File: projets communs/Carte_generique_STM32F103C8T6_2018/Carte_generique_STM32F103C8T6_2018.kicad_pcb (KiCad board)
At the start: 2 copper layers, 26 parts, among them J1 Conn_01x20_Female, J2 Alim puissance, J3 Alim logique, J4 Conn_01x20_Female, J5 PWM input, J6 PWM output, J7 QEI, J8 Liaison serie, Q1 PMF370XN, Q2 2N7000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

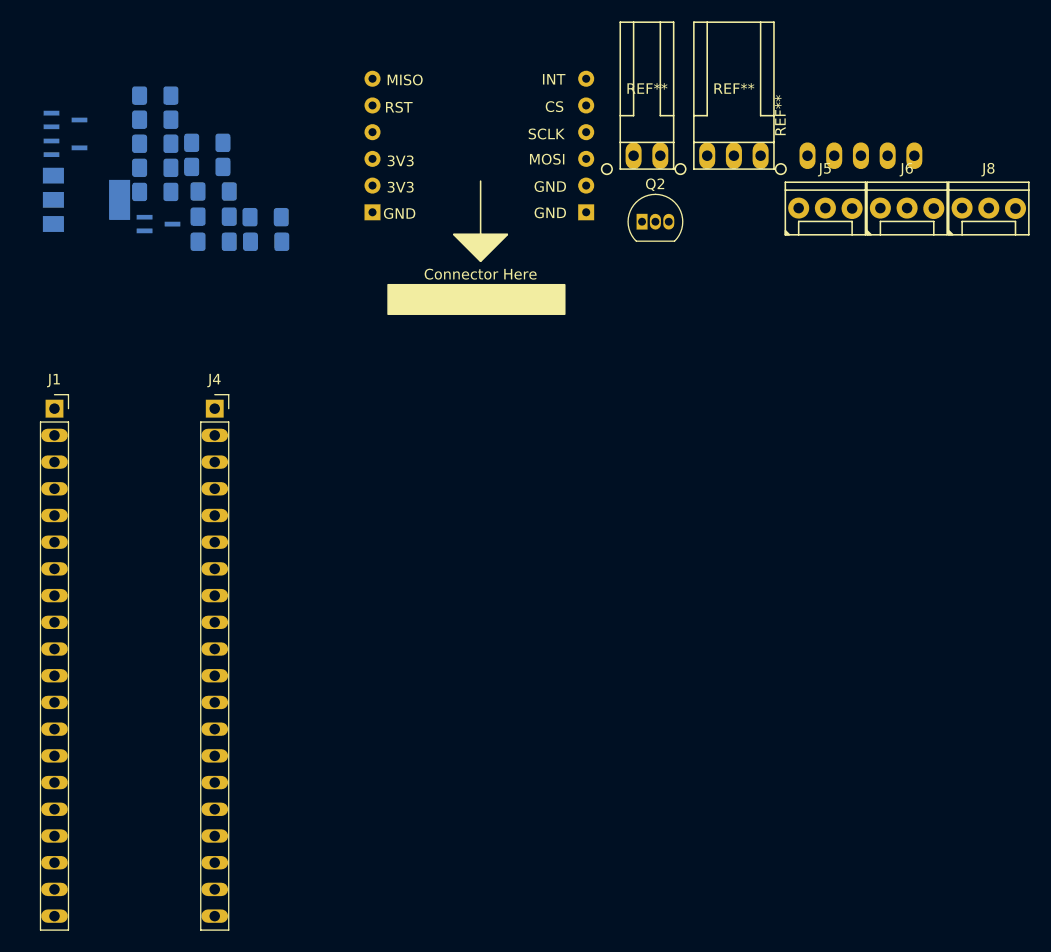
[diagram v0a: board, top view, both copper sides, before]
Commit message: added the blackpill actual courtyard
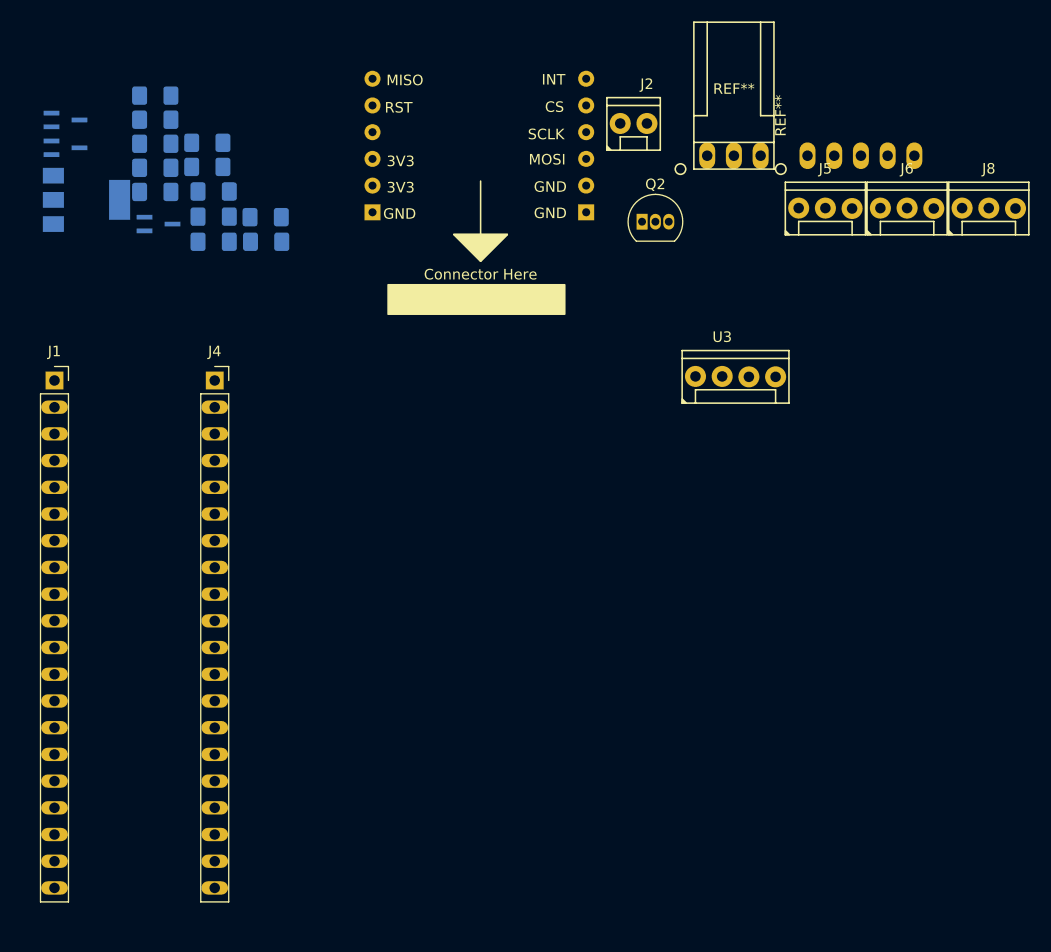
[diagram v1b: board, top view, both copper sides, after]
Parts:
- added U3: servo_connector, @Robot:HE14-4-straight, F.Cu at (180.3, 74.9)
- J2: footprint @Robot:HE14-2_horizontal -> @Robot:HE14-2-straight
- R2, R3: value R -> 10k
- moved J1 2.68 mm to (116.8, 76.1)
- moved J4 2.68 mm to (132.1, 76.1)
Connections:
- J1 pad 20: +3V3 -> Net-(J1-Pad20)
- J4 pad 3: +3V3 -> Net-(J4-Pad3)
- Q3 pad 1: /TX -> /led_communication

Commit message: changed the power connector footprint
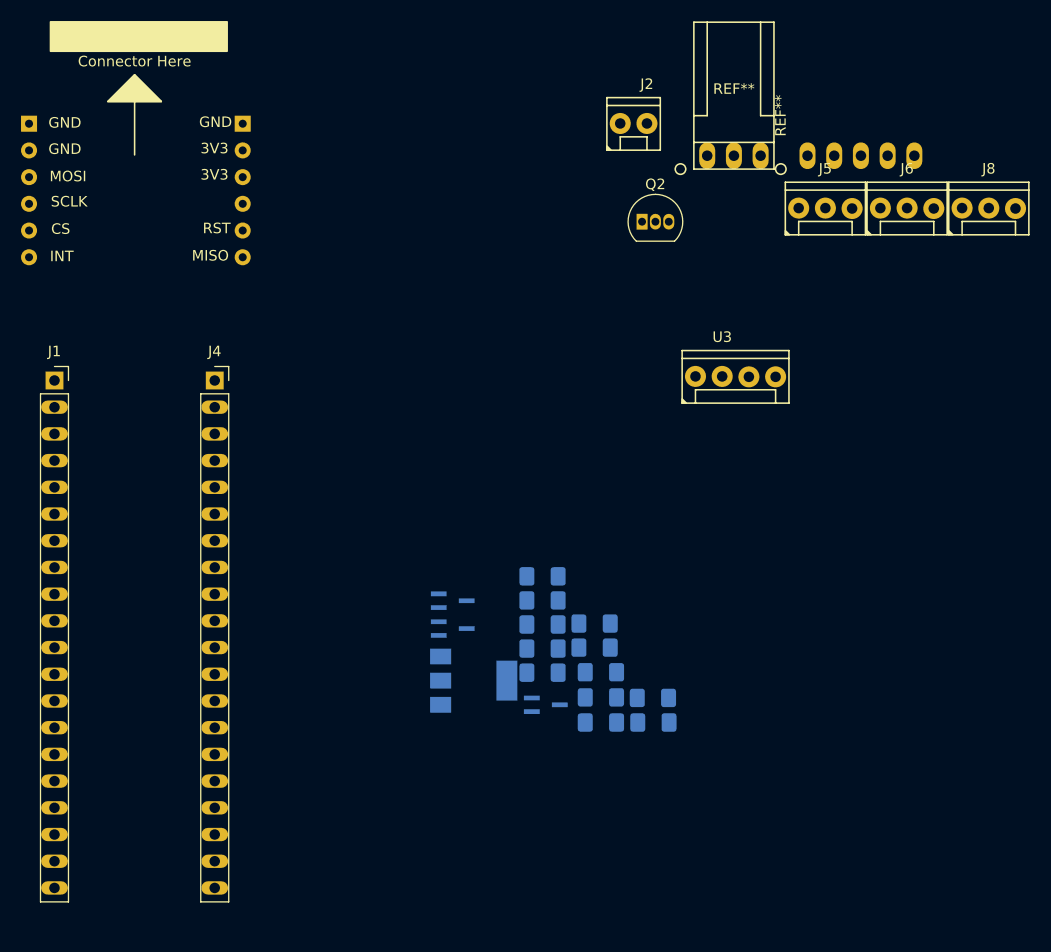
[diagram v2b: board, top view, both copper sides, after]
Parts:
- moved C2 58.7 mm to (163.3, 101.6)
- moved R4 58.7 mm to (163.3, 97.0)
- moved C1 58.7 mm to (163.3, 103.8)
- moved R1 58.7 mm to (163.3, 99.3)
- moved R5 58.7 mm to (163.3, 94.7)
- moved R6 58.7 mm to (173.8, 106.2)
- moved D1 58.7 mm to (168.8, 108.6)
- moved D2 58.7 mm to (173.8, 108.6)
- moved D3 58.7 mm to (168.8, 106.2)
- moved D4 58.7 mm to (168.8, 103.8)
- moved Q1 58.7 mm to (163.6, 106.9)
- moved Q3 58.7 mm to (154.7, 99.7)
- moved Q4 58.7 mm to (154.7, 97.0)
- moved U1 58.7 mm to (156.7, 104.6)
- moved R3 58.7 mm to (168.2, 99.2)
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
